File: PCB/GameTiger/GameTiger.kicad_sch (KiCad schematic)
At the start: 52 parts, among them J1 USB_B_Micro, U1 RP2040, U2 NCP1117-3.3_SOT223, U3 W25Q128JVS, U4 PAM8302A, Y1 ABLS-12MHZ-B4-T

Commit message: PCB Schematic for V2.0 is completed
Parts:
- removed C?: 10μF, symbol Device:C_Small
- removed C?: 0.1μF, symbol Device:C_Small
- removed J1: USB_B_Micro, symbol Connector:USB_B_Micro
- removed RN?: 47KΩ, Resistor_THT:R_Array_SIP6, symbol Device:R_Network05
- removed U2: NCP1117-3.3_SOT223, Package_TO_SOT_SMD:SOT-223-3_TabPin2, symbol Regulator_Linear:NCP1117-3.3_SOT223
- added C19, C23: 10μF, symbol Device:C_Small
- added D1: MBR0540, Diode_SMD:D_SOD-123, symbol Diode:MBR0540
- added D2: Orange, symbol Device:LED_Small
- added J1: USB_C_Receptacle_USB2.0, symbol Connector:USB_C_Receptacle_USB2.0
- added J3: LCD Display, symbol Connector_Generic:Conn_01x12
- added Q3: DMG3415, Adafruit Feather RP2040:SOT23-R, symbol Adafruit Feather RP2040-eagle-import:MOSFET-P
- added R10, R12, R13: 10KΩ, symbol Device:R_Small
- added R11, R14, R15: 5.1KΩ, symbol Device:R_Small
- added Reset1: SW_Push, symbol Switch:SW_Push
- added U2: MCP73831-2-OT, Package_TO_SOT_SMD:SOT-23-5, symbol Battery_Management:MCP73831-2-OT
- added U5: AP2112K-3.3, Package_TO_SOT_SMD:SOT-23-5, symbol Regulator_Linear:AP2112K-3.3
- C10, C8: value 1μF -> 100nF
- C6, C9: value 100nF -> 1μF
- gave numbers to parts that had none: 1
- renumbered A to A1, B to B1, Boot to Boot1, Down to Down1, Left to Left1, Right to Right1, Select to Select1, Start to Start1, Up to Up1
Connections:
- net +1V1: now also C11.1, C13.1, C9.1; no longer C6.1, C7.1, C8.1
- net +3.3V: now also C6.1, C7.1, C8.1, C19.2, C23.2, J3.3 (Pin_3), J3.4 (Pin_4), U5.5 (VOUT); no longer C11.1, C13.1, C22.2, C4.1, C9.1, R6.2, U4.6 (VDD)
- net GND: now also C4.1, C19.1, C23.1, J1.A1 (GND), J1.A12 (GND), J1.B1 (GND), J1.B12 (GND), J3.1 (Pin_1), J3.12 (Pin_12), J3.2 (Pin_2), J3.5 (Pin_5), J3.6 (Pin_6), R10.2, R11.2, R14.2, R15.2, Reset1.1, U2.2 (V_{SS}), U5.2 (GND); no longer C4.2
- net POWER_USB_DM: now also J1.A7 (D-), J1.B7 (D-)
- net POWER_USB_DP: now also J1.A6 (D+), J1.B6 (D+)
- net VBUS: now also D1.2 (A), D2.2 (A), J1.A4 (VBUS), J1.A9 (VBUS), J1.B4 (VBUS), J1.B9 (VBUS), Q3.1 (G), R10.1, U2.4 (V_{DD}); no longer C1.1
- net LCD_DC: now reaches U1.11 (GPIO8)
- net LCD_DC: now also J3.7 (Pin_7)
- net LCD_CS: now reaches U1.12 (GPIO9)
- net LCD_CS: now also J3.8 (Pin_8)
- net LCD_CLK: now reaches U1.13 (GPIO10)
- net LCD_CLK: now also J3.9 (Pin_9)
- net LCD_DATA: now reaches U1.14 (GPIO11)
- net LCD_DATA: now also J3.10 (Pin_10)
- net at U1.26 (RUN): now also Reset1.2
- net LCD_RESET: now reaches U1.9 (GPIO7)
- net LCD_RESET: now also J3.11 (Pin_11)
- new net: J1.B5 (CC2), R14.1
- new net: J1.A5 (CC1), R15.1
- new net: R12.1, U5.3 (EN)
- new net: C1.1, D1.1 (K), Q3.2 (S), R12.2, U5.1 (VIN)
- new net: R11.1, U2.5 (PROG)
- new net: D2.1 (K), R13.1
- new net: R13.2, U2.1 (STAT)
- new net VBAT: C22.2, C4.2, Q3.3 (D), R6.2, U2.3 (V_{BAT}), U4.6 (VDD)
- no-connect marks 3 -> 2
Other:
- note added: "Decoupling capacitors"
- note added: "LCD Display Connector"
- note added: "Power & Filtering"
- note added: "USB-C Connector"
- moved on the sheet: A1, B1, Boot1, C17, C18, C2, C20, C21, C22, C3, C5, Down1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

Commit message: Updated Schematics to correct footprints
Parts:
- removed J2: ~, symbol Connector:Micro_SD_Card_Det2
- removed J3: LCD Display, symbol Connector_Generic:Conn_01x12
- added AE1: Antenna, Connector_Pin:Pin_D1.0mm_L10.0mm, symbol Device:Antenna
- added J2: 503398-1892, 503398-1892:MOLEX_503398-1892, symbol 503398-1892:503398-1892
- added J3: LCD Display, Connector_FFC-FPC:TE_1-1734839-5_1x15-1MP_P0.5mm_Horizontal, symbol Connector_Generic:Conn_01x15
- added U6: PCF8574TS, Package_SO:SSOP-20_4.4x6.5mm_P0.65mm, symbol Interface_Expansion:PCF8574TS
- added U7: ~, Waveshare:Core SX1262, symbol Waveshare:Core-SX1262
- A1, B1, Down1, Left1, Right1, Up1: footprint (none) -> Button_Switch_THT:SW_PUSH-12mm_Wuerth-430476085716
- Boot1, Reset1: footprint (none) -> Button_Switch_SMD:SW_SPST_B3U-1000P
- C1, C19, C22, C23, C4: footprint (none) -> Capacitor_SMD:C_0805_2012Metric
- C10, C11, C12, C13, C14, C15, C16, C17, C18, C2, C20, C21, C3, C5, C6, C7, C8, C9: footprint (none) -> Capacitor_SMD:C_0402_1005Metric
- D2: footprint (none) -> LED_SMD:LED_0402_1005Metric
- FB1, FB2: footprint (none) -> PCM_Ferrite_SMD_AKL:Ferrite_0402_1005Metric
- J1: footprint (none) -> Connector_USB:USB_C_Receptacle_HRO_TYPE-C-31-M-12
- Q3: footprint Adafruit Feather RP2040:SOT23-R -> Package_TO_SOT_SMD:SOT-23
- R1, R10, R11, R12, R13, R14, R15, R2, R3, R4, R5, R6, R8, R9: footprint (none) -> Resistor_SMD:R_0402_1005Metric
- R7: value R_Trim -> 10KΩ; footprint (none) -> Potentiometer_SMD:Potentiometer_Bourns_3314G_Vertical
- Select1, Start1: footprint (none) -> Button_Switch_THT:SW_PUSH_6mm
- Y1: footprint (none) -> Crystal:Crystal_SMD_2520-4Pin_2.5x2.0mm
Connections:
- net +3.3V: now also J2.4 (VDD), J3.2 (Pin_2), J3.4 (Pin_4), J3.5 (Pin_5), U6.5 (VDD), U7.8 (3x3)
- net Audio_PWM: now also U1.28 (GPIO17); no longer U1.31 (GPIO20)
- net GND: now also J1.S1 (SHIELD), J2.6 (VSS), J2.9 (VSS), J2.P1 (SHIELD), J2.P2 (SHIELD), J2.P3 (SHIELD), J2.P4 (SHIELD), J3.1 (Pin_1), J3.11 (Pin_11), J3.13 (Pin_13), J3.15 (Pin_15), J3.3 (Pin_3), J3.7 (Pin_7), J3.9 (Pin_9), U6.15 (VSS), U6.6 (A0), U6.7 (A1), U6.9 (A2), U7.1 (GND), U7.10 (GND), U7.2 (GND), U7.7 (GND)
- net KYBD_A: now also U6.16 (P4); no longer U1.27 (GPIO16)
- net KYBD_B: now also U6.17 (P5); no longer U1.28 (GPIO17)
- net KYBD_DOWN: now also U6.11 (P1); no longer U1.16 (GPIO13)
- net KYBD_LEFT: now also U6.12 (P2); no longer U1.17 (GPIO14)
- net KYBD_RIGHT: now also U6.14 (P3); no longer U1.18 (GPIO15)
- net KYBD_SELECT: now also U6.19 (P6); no longer U1.29 (GPIO18)
- net KYBD_START: now also U6.20 (P7); no longer U1.30 (GPIO19)
- net KYBD_UP: now also U6.10 (P0); no longer U1.15 (GPIO12)
- net LCD_CLK: now also U1.17 (GPIO14), J3.10 (Pin_10); no longer U1.13 (GPIO10)
- net LCD_CS: now also U1.16 (GPIO13), J3.6 (Pin_6); no longer U1.12 (GPIO9)
- net LCD_DATA: now also U1.18 (GPIO15), J3.8 (Pin_8); no longer U1.14 (GPIO11)
- net LCD_DC: now also U1.15 (GPIO12), J3.14 (Pin_14); no longer U1.11 (GPIO8)
- net LCD_RESET: now also U1.27 (GPIO16), J3.12 (Pin_12); no longer U1.9 (GPIO7)
- net MicroSD_CLK: now also J2.5 (CLK)
- net MicroSD_CS: now also J2.2 (CD/DAT3^2)
- net MicroSD_MISO: now also J2.7 (DAT0)
- net MicroSD_MOSI: now also J2.3 (CMD)
- net SX1262_DIO1: now reaches U1.7 (GPIO5)
- net SX1262_DIO1: now also U7.6 (DIO1)
- net SX1262_RESET: now reaches U1.8 (GPIO6)
- net SX1262_RESET: now also U7.15 (RESET)
- net MicroSD_DET renamed MicroSD_DETECT
- net MicroSD_DETECT: now also J2.10 (DETECT_SWITCH)
- new net: AE1.1 (A), U7.9 (ANT)
- new net KYBD_INT: U1.31 (GPIO20), U6.1 (~{INT})
- new net KYBD_SCL: U1.30 (GPIO19), U6.2 (SCL)
- new net KYBD_SDA: U1.29 (GPIO18), U6.4 (SDA)
- new net SX1262_BUSY: U1.9 (GPIO7), U7.16 (BUSY)
- new net SX1262_CLK: U1.13 (GPIO10), U7.12 (CLK)
- new net SX1262_CS: U1.12 (GPIO9), U7.11 (CS)
- new net SX1262_MISO: U1.11 (GPIO8), U7.14 (MISO)
- new net SX1262_MOSI: U1.14 (GPIO11), U7.13 (MOSI)
- no-connect marks 2 -> 5
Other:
- note added: "8-Bit I/O Expander"
- note added: "Core SX1262"
- moved on the sheet: Q3, R12

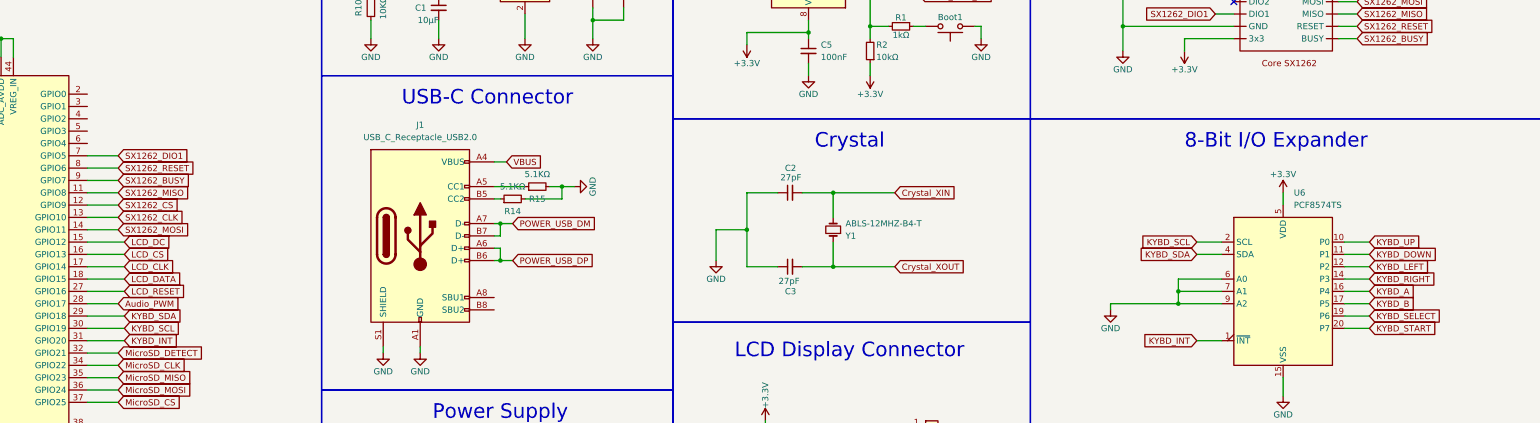
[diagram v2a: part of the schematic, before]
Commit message: PCB layout completed with all tracks and connections
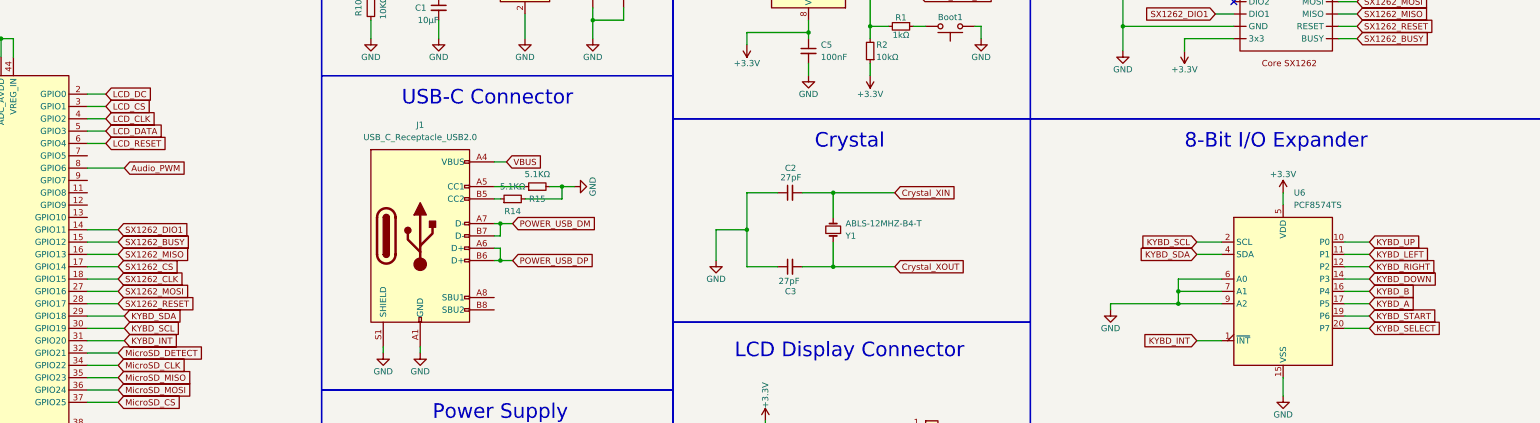
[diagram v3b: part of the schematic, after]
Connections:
- net Audio_PWM: now also U1.8 (GPIO6); no longer U1.28 (GPIO17)
- net KYBD_A: now also U6.17 (P5); no longer U6.16 (P4)
- net KYBD_B: now also U6.16 (P4); no longer U6.17 (P5)
- net KYBD_DOWN: now also U6.14 (P3); no longer U6.11 (P1)
- net KYBD_LEFT: now also U6.11 (P1); no longer U6.12 (P2)
- net KYBD_RIGHT: now also U6.12 (P2); no longer U6.14 (P3)
- net KYBD_SELECT: now also U6.20 (P7); no longer U6.19 (P6)
- net KYBD_START: now also U6.19 (P6); no longer U6.20 (P7)
- net LCD_CLK: now also U1.4 (GPIO2); no longer U1.17 (GPIO14)
- net LCD_CS: now also U1.3 (GPIO1); no longer U1.16 (GPIO13)
- net LCD_DATA: now also U1.5 (GPIO3); no longer U1.18 (GPIO15)
- net LCD_DC: now also U1.2 (GPIO0); no longer U1.15 (GPIO12)
- net LCD_RESET: now also U1.6 (GPIO4); no longer U1.27 (GPIO16)
- net SX1262_BUSY: now also U1.15 (GPIO12); no longer U1.9 (GPIO7)
- net SX1262_CLK: now also U1.18 (GPIO15); no longer U1.13 (GPIO10)
- net SX1262_CS: now also U1.17 (GPIO14); no longer U1.12 (GPIO9)
- net SX1262_DIO1: now also U1.14 (GPIO11); no longer U1.7 (GPIO5)
- net SX1262_MISO: now also U1.16 (GPIO13); no longer U1.11 (GPIO8)
- net SX1262_MOSI: now also U1.27 (GPIO16); no longer U1.14 (GPIO11)
- net SX1262_RESET: now also U1.28 (GPIO17); no longer U1.8 (GPIO6)

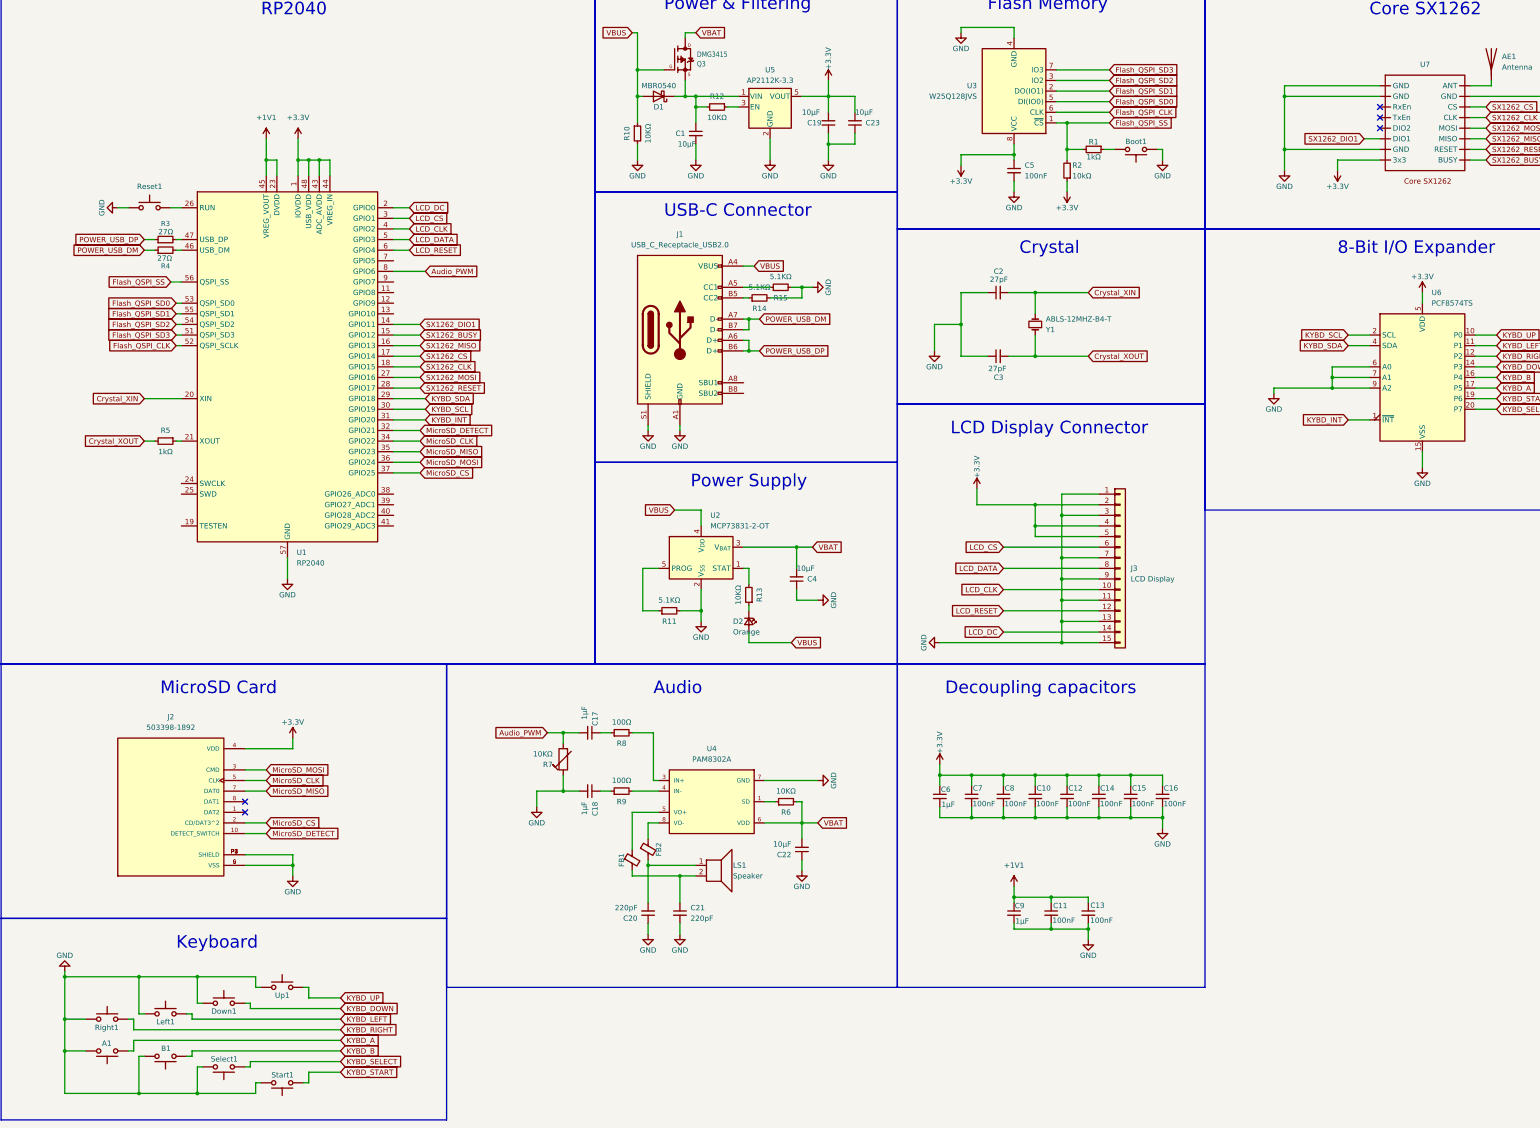
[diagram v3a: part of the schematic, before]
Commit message: Added more details on the PCB components
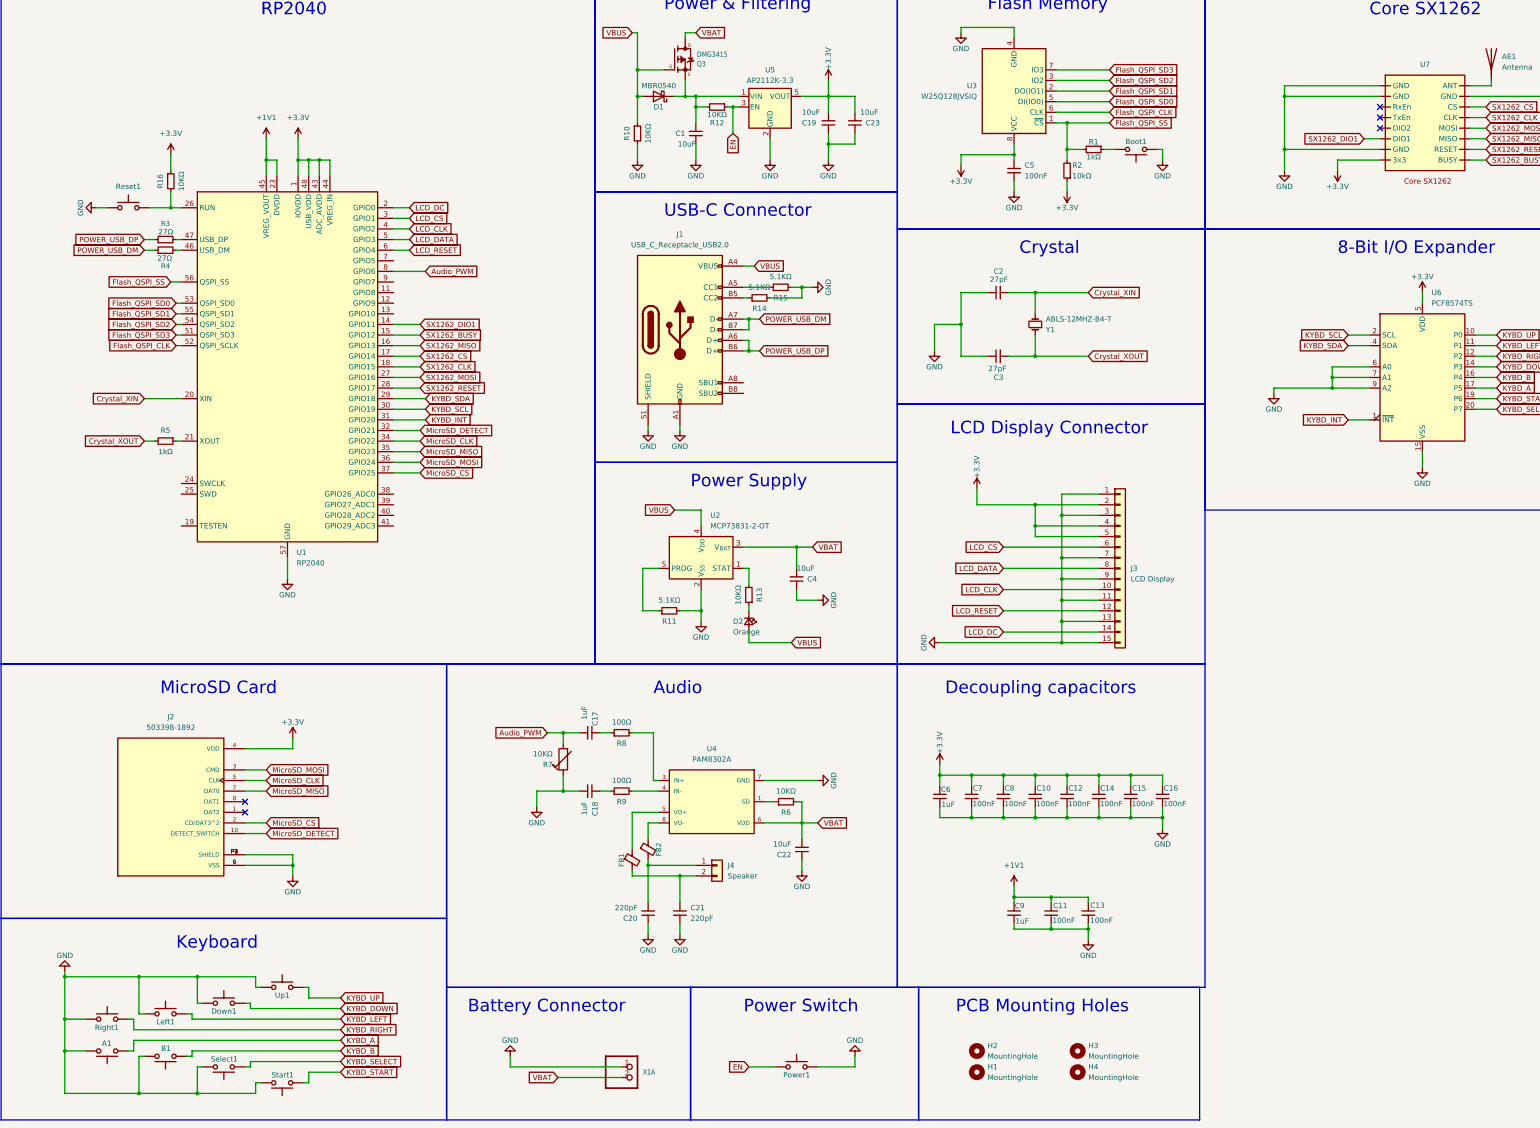
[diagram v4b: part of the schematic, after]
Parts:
- removed LS1: Speaker, symbol Device:Speaker
- added H1, H2, H3, H4: MountingHole, MountingHole:MountingHole_2.2mm_M2, symbol Mechanical:MountingHole
- added J4: Speaker, Connector_Wire:SolderWire-0.5sqmm_1x02_P4.6mm_D0.9mm_OD2.1mm, symbol Connector_Generic:Conn_01x02
- added Power1: SW_Push, Button_Switch_SMD:SW_SPDT_CK-JS102011SAQN, symbol Switch:SW_Push
- added R16: 10KΩ, Resistor_SMD:R_0402_1005Metric, symbol Device:R_Small
- added X1: ~, Connector_JST:JST_PH_S2B-PH-SM4-TB_1x02-1MP_P2.00mm_Horizontal, symbol GameTiger-eagle-import:CON_JST_PH_2PIN_MT_BATT
- Boot1, Reset1: Manufacturer (none) -> Omron Electronics; Mfr.Part # (none) -> B3U-1000P; Size (none) -> SMD,2.5x3mm
- C1, C19, C22, C23, C4: value 10μF -> 10uF; Material (none) -> X5R; Size (none) -> 0805_2012Metric; Tolerance (none) -> 10%; Voltage (none) -> 16v
- C10, C11, C12, C13, C14, C15, C16, C5, C7, C8: Material (none) -> X7R; Size (none) -> 0402_1005Metric; Tolerance (none) -> 10%; Voltage (none) -> 25v
- C17, C18, C6, C9: value 1μF -> 1uF; Material (none) -> X6S; Size (none) -> 0402_1005Metric; Tolerance (none) -> 10%; Voltage (none) -> 10V
- C2, C3: Material (none) -> C0G; Size (none) -> 0402_1005Metric; Tolerance (none) -> 5%; Voltage (none) -> 50v
- C20, C21: footprint Capacitor_SMD:C_0402_1005Metric -> Capacitor_SMD:C_0805_2012Metric; Material (none) -> C0G; Size (none) -> 0805_2012Metric; Tolerance (none) -> 5%; Voltage (none) -> 50v
- D1: Manuf. Part # (none) -> MBR0540T1G; Manufacturer (none) -> FUXINSEMI; Size (none) -> SOD-123
- FB1, FB2: footprint PCM_Ferrite_SMD_AKL:Ferrite_0402_1005Metric -> PCM_Ferrite_SMD_AKL:Ferrite_0805_2012Metric; Manuf. Part # (none) -> BLM21AG102BH1D; Manufacturer (none) -> Murata Electronics; Size (none) -> 0805
- J1: Manuf. Part # (none) -> GT-USB-7010ASV; Manufacturer (none) -> G-Switch; Size (none) -> Type-C
- J2: MANUFACTURER molex -> (none); Manuf. Part # (none) -> 5033981892; Manufacturer (none) -> MOLEX; PARTREV 0 -> (none); STANDARD MANUFACTURER RECOMMENDATIONS -> (none)
- Q3: Manuf. Part # (none) -> DMG3415U-7; Manufacturer (none) -> Diodes Incorporated; Size (none) -> SOT-23
- R1, R10, R11, R12, R13, R14, R15, R2, R3, R4, R5, R6, R8, R9: Power (none) -> 63mW; Size (none) -> 0402_1005Metric
- R7: footprint Potentiometer_SMD:Potentiometer_Bourns_3314G_Vertical -> Potentiometer_SMD:Potentiometer_Bourns_TC33X_Vertical; Manuf. Part # (none) -> TC33X-2-103E; Manufacturer (none) -> Bourns; Size (none) -> SMD 3MM
- U1: Manufacturer (none) -> Raspberry Pi; Mfr.Part # (none) -> RP2040; Size (none) -> QFN56
- U2: Manuf. Part # (none) -> MCP73831T-2ACI/OT; Manufacturer (none) -> Microchip Tech; Size (none) -> SOT-23-5
- U3: value W25Q128JVS -> W25Q128JVSIQ; Manuf. Part # (none) -> W25Q128JVSIQ; Manufacturer (none) -> Winbond; Size (none) -> SOIC-8 208-mil
- U4: footprint PAM8302A -> PAM8302A:PAM8302A; Manuf. Part # (none) -> PAM8302AASCR; Manufacturer (none) -> Diodes Incorporated; Size (none) -> MSOP-8
- U5: Manuf. Part # (none) -> AP2112K-3.3TRG1; Manufacturer (none) -> Diodes Incorporated; Size (none) -> SOT-23-5
- U6: Manuf. Part # (none) -> PCF8574TS; Manufacturer (none) -> NXP Semicon; Size (none) -> SSOP20
- Y1: Manuf. Part # (none) -> SX2B12.000F1210F30; Manufacturer (none) -> Shenzhen SCTF Elec; Size (none) -> SMD2520-4P
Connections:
- net +3.3V: now also R16.1
- net GND: now also Power1.2, X1.1
- net VBAT: now also X1.2
- net at C20.2, FB2.2: now also J4.1 (Pin_1)
- net EN: now reaches R12.1, U5.3 (EN)
- net EN: now also Power1.1
- net at C21.1, FB1.2: now also J4.2 (Pin_2)
- net at Reset1.2, U1.26 (RUN): now also R16.2
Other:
- note added: "Battery Connector"
- note added: "PCB Mounting Holes"
- note added: "Power Switch"
- moved on the sheet: Reset1

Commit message: PCB layout and component reference completed
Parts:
- A1, B1, Down1, Left1, Right1, Up1: footprint Button_Switch_THT:SW_PUSH-12mm_Wuerth-430476085716 -> Button_Switch_SMD:SW_Push_1P1T_NO_CK_PTS125Sx43PSMTR; Manufacturer (none) -> C&K; Mfr.Part # (none) -> PTS125SJM73PSMTR2LFS; Size (none) -> SMD,12x12mm
- J3: Manuf. Part # (none) -> AFC07-S15FCA-00; Manufacturer (none) -> JUSHUO; Size (none) -> SMD,P=0.5mm
- R1, R5: value 1kΩ -> 1k
- R10, R12, R13, R16, R6, R7: value 10KΩ -> 10K
- R11, R14, R15: value 5.1KΩ -> 5.1K
- R2: value 10kΩ -> 10K
- R3, R4: value 27Ω -> 27
- R8, R9: value 100Ω -> 100
- Select1, Start1: footprint Button_Switch_THT:SW_PUSH_6mm -> Button_Switch_SMD:SW_Push_1P1T_NO_CK_KMR2; Manufacturer (none) -> C&K; Mfr.Part # (none) -> KMR223GLFG; Size (none) -> SMD
- U7: now left out of the parts list
